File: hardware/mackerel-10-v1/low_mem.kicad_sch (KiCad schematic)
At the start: 8 parts, among them U3 SST39SF040, U4 AS6C4008-55PCN, U5 SST39SF040, U6 AS6C4008-55PCN

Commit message: Another layout plan
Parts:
- removed C1, C2, C3, C4: 0.1uF, Capacitor_THT:C_Disc_D4.7mm_W2.5mm_P5.00mm, symbol Device:C

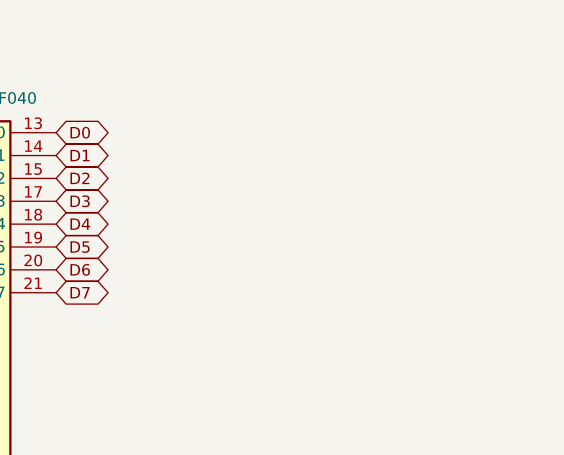
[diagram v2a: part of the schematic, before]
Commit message: half routed
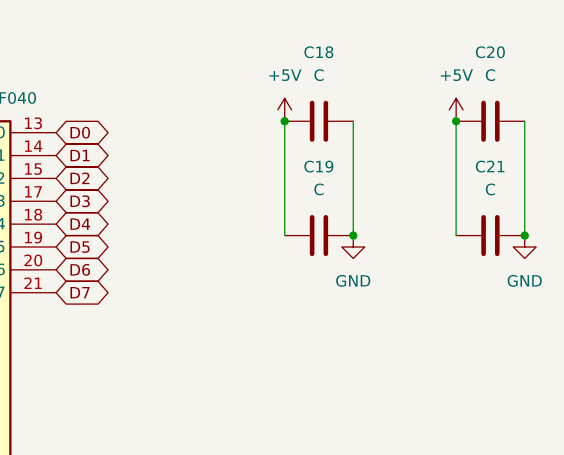
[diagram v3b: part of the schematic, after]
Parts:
- added C18, C19, C20, C21: C, Capacitor_THT:C_Disc_D4.3mm_W1.9mm_P5.00mm, symbol Device:C
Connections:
- net +5V: now also C18.1, C19.1, C20.1, C21.1
- net GND: now also C18.2, C19.2, C20.2, C21.2

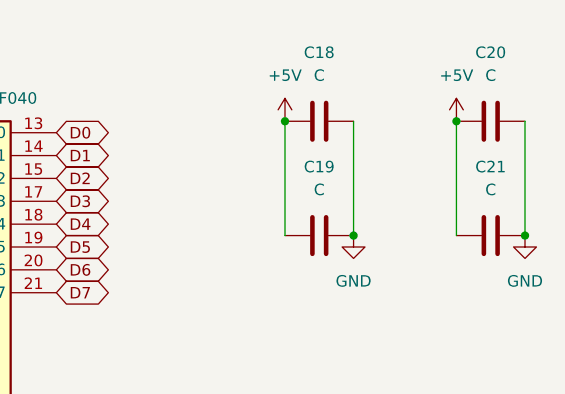
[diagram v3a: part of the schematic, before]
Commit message: Remove BERR from CPLD
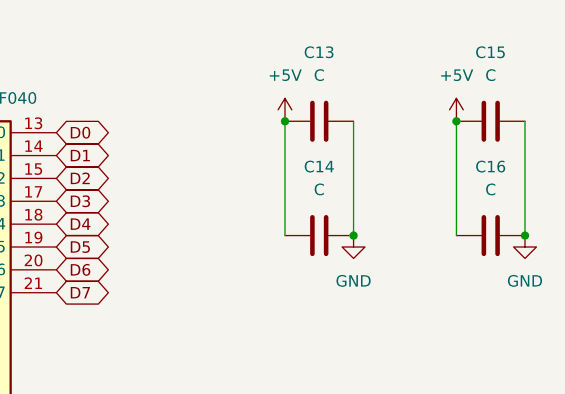
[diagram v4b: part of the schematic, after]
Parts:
- renumbered C18 to C13, C19 to C14, C20 to C15, C21 to C16
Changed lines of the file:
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@@
 		(dnp no)
 		(fields_autoplaced yes)
-		(property "Reference" "#PWR016"
+		(property "Reference" "#PWR025"
 			(at 128.27 34.29 0)
 			(effects
@@
 			(project "mackerel-10-v1"
 				(path "/0a8f74be-008b-4256-a2d9-73a458311ea0/94b238fa-f0c8-40a8-9ec2-3b22cf78cf25"
-					(reference "#PWR016")
+					(reference "#PWR025")
 					(unit 1)
 				)
@@
 		(dnp no)
 		(fields_autoplaced yes)
-		(property "Reference" "#PWR012"
+		(property "Reference" "#PWR021"
 			(at 49.53 111.76 0)
 			(effects
@@
 			(project "mackerel-10-v1"
 				(path "/0a8f74be-008b-4256-a2d9-73a458311ea0/94b238fa-f0c8-40a8-9ec2-3b22cf78cf25"
-					(reference "#PWR012")
+					(reference "#PWR021")
 					(unit 1)
 				)
@@
 		(dnp no)
 		(fields_autoplaced yes)
-		(property "Reference" "#PWR018"
+		(property "Reference" "#PWR027"
 			(at 128.27 128.27 0)
 			(effects
@@
 			(project "mackerel-10-v1"
 				(path "/0a8f74be-008b-4256-a2d9-73a458311ea0/94b238fa-f0c8-40a8-9ec2-3b22cf78cf25"
-					(reference "#PWR018")
+					(reference "#PWR027")
 					(unit 1)
 				)
@@
 		(dnp no)
 		(fields_autoplaced yes)
-		(property "Reference" "#PWR019"
+		(property "Reference" "#PWR028"
 			(at 128.27 191.77 0)
 			(effects
@@
 			(project "mackerel-10-v1"
 				(path "/0a8f74be-008b-4256-a2d9-73a458311ea0/94b238fa-f0c8-40a8-9ec2-3b22cf78cf25"
-					(reference "#PWR019")
+					(reference "#PWR028")
 					(unit 1)
 				)
@@
 		(dnp no)
 		(fields_autoplaced yes)
-		(property "Reference" "#PWR013"
+		(property "Reference" "#PWR022"
 			(at 49.53 128.27 0)
 			(effects
@@
 			(project "mackerel-10-v1"
 				(path "/0a8f74be-008b-4256-a2d9-73a458311ea0/94b238fa-f0c8-40a8-9ec2-3b22cf78cf25"
-					(reference "#PWR013")
+					(reference "#PWR022")
 					(unit 1)
 				)
@@
 		(dnp no)
 		(fields_autoplaced yes)
-		(property "Reference" "#PWR059"
+		(property "Reference" "#PWR031"
 			(at 187.96 39.37 0)
 			(effects
@@
 			(project "mackerel-10-v1"
 				(path "/0a8f74be-008b-4256-a2d9-73a458311ea0/94b238fa-f0c8-40a8-9ec2-3b22cf78cf25"
-					(reference "#PWR059")
+					(reference "#PWR031")
 					(unit 1)
 				)
@@
 		(dnp no)
 		(fields_autoplaced yes)
-		(property "Reference" "#PWR015"
+		(property "Reference" "#PWR024"
 			(at 104.14 91.44 0)
 			(effects
@@
 			(project "mackerel-10-v1"
 				(path "/0a8f74be-008b-4256-a2d9-73a458311ea0/94b238fa-f0c8-40a8-9ec2-3b22cf78cf25"
-					(reference "#PWR015")
+					(reference "#PWR024")
 					(unit 1)
 				)
@@
 		(dnp no)
 		(fields_autoplaced yes)
-		(property "Reference" "C21"
+		(property "Reference" "C16"
 			(at 191.77 40.64 90)
 			(effects
@@
 			(project "mackerel-10-v1"
 				(path "/0a8f74be-008b-4256-a2d9-73a458311ea0/94b238fa-f0c8-40a8-9ec2-3b22cf78cf25"
-					(reference "C21")
+					(reference "C16")
 					(unit 1)
 				)
@@
 		(dnp no)
 		(fields_autoplaced yes)
-		(property "Reference" "#PWR017"
+		(property "Reference" "#PWR026"
 			(at 128.27 113.03 0)
 			(effects
@@
 			(project "mackerel-10-v1"
 				(path "/0a8f74be-008b-4256-a2d9-73a458311ea0/94b238fa-f0c8-40a8-9ec2-3b22cf78cf25"
-					(reference "#PWR017")
+					(reference "#PWR026")
 					(unit 1)
 				)
@@
 		(dnp no)
 		(fields_autoplaced yes)
-		(property "Reference" "#PWR010"
+		(property "Reference" "#PWR019"
 			(at 25.4 91.44 0)
 			(effects
@@
 			(project "mackerel-10-v1"
 				(path "/0a8f74be-008b-4256-a2d9-73a458311ea0/94b238fa-f0c8-40a8-9ec2-3b22cf78cf25"
-					(reference "#PWR010")
+					(reference "#PWR019")
 					(unit 1)
 				)
@@
 		(dnp no)
 		(fields_autoplaced yes)
-		(property "Reference" "C20"
+		(property "Reference" "C15"
 			(at 191.77 27.94 90)
 			(effects
@@
 			(project "mackerel-10-v1"
 				(path "/0a8f74be-008b-4256-a2d9-73a458311ea0/94b238fa-f0c8-40a8-9ec2-3b22cf78cf25"
-					(reference "C20")
+					(reference "C15")
 					(unit 1)
 				)
@@
 		(dnp no)
 		(fields_autoplaced yes)
-		(property "Reference" "#PWR014"
+		(property "Reference" "#PWR023"
 			(at 49.53 191.77 0)
 			(effects
@@
 			(project "mackerel-10-v1"
 				(path "/0a8f74be-008b-4256-a2d9-73a458311ea0/94b238fa-f0c8-40a8-9ec2-3b22cf78cf25"
-					(reference "#PWR014")
+					(reference "#PWR023")
 					(unit 1)
 				)
@@
 		(dnp no)
 		(fields_autoplaced yes)
-		(property "Reference" "#PWR050"
+		(property "Reference" "#PWR029"
 			(at 168.91 39.37 0)
 			(effects
@@
 			(project "mackerel-10-v1"
 				(path "/0a8f74be-008b-4256-a2d9-73a458311ea0/94b238fa-f0c8-40a8-9ec2-3b22cf78cf25"
-					(reference "#PWR050")
+					(reference "#PWR029")
 					(unit 1)
 				)
@@
 		(dnp no)
 		(fields_autoplaced yes)
-		(property "Reference" "#PWR060"
+		(property "Reference" "#PWR032"
 			(at 195.58 54.61 0)
 			(effects
@@
 			(project "mackerel-10-v1"
 				(path "/0a8f74be-008b-4256-a2d9-73a458311ea0/94b238fa-f0c8-40a8-9ec2-3b22cf78cf25"
-					(reference "#PWR060")
+					(reference "#PWR032")
 					(unit 1)
 				)
@@
 		(dnp no)
 		(fields_autoplaced yes)
-		(property "Reference" "#PWR011"
+		(property "Reference" "#PWR020"
 			(at 49.53 34.29 0)
 			(effects
@@
 			(project "mackerel-10-v1"
 				(path "/0a8f74be-008b-4256-a2d9-73a458311ea0/94b238fa-f0c8-40a8-9ec2-3b22cf78cf25"
-					(reference "#PWR011")
+					(reference "#PWR020")
 					(unit 1)
 				)
@@
 		(dnp no)
 		(fields_autoplaced yes)
-		(property "Reference" "#PWR051"
+		(property "Reference" "#PWR030"
 			(at 176.53 54.61 0)
 			(effects
@@
 			(project "mackerel-10-v1"
 				(path "/0a8f74be-008b-4256-a2d9-73a458311ea0/94b238fa-f0c8-40a8-9ec2-3b22cf78cf25"
-					(reference "#PWR051")
+					(reference "#PWR030")
 					(unit 1)
 				)
@@
 		(dnp no)
 		(fields_autoplaced yes)
-		(property "Reference" "C18"
+		(property "Reference" "C13"
 			(at 172.72 27.94 90)
 			(effects
@@
 			(project "mackerel-10-v1"
 				(path "/0a8f74be-008b-4256-a2d9-73a458311ea0/94b238fa-f0c8-40a8-9ec2-3b22cf78cf25"
-					(reference "C18")
+					(reference "C13")
 					(unit 1)
 				)
@@
 		(dnp no)
 		(fields_autoplaced yes)
-		(property "Reference" "C19"
+		(property "Reference" "C14"
 			(at 172.72 40.64 90)
 			(effects
@@
 			(project "mackerel-10-v1"
 				(path "/0a8f74be-008b-4256-a2d9-73a458311ea0/94b238fa-f0c8-40a8-9ec2-3b22cf78cf25"
-					(reference "C19")
-					(unit 1)
-				)
+					(reference "C14")
+					(unit 1)
+				)

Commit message: Mackerel-10 v1.1 release PCB
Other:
- title: Mackerel-10 SBC v1 -> Mackerel-10 SBC v1.1
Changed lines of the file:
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@@
 	(paper "A")
 	(title_block
-		(title "Mackerel-10 SBC v1")
-		(date "2024-09-23")
-		(rev "1.0a")
+		(title "Mackerel-10 SBC v1.1")
+		(date "2024-10-27")
+		(rev "1.1a")
 		(company "Colin Maykish")
 	)

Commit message: Add Mackerel-10 v1.1 BOM
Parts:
- C13, C14, C15, C16: value C -> 0.1uF
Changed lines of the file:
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@@
 			)
 		)
-		(property "Value" "C"
+		(property "Value" "0.1uF"
 			(at 191.77 43.18 90)
 			(effects
@@
 			)
 		)
-		(property "Value" "C"
+		(property "Value" "0.1uF"
 			(at 191.77 30.48 90)
 			(effects
@@
 			)
 		)
-		(property "Value" "C"
+		(property "Value" "0.1uF"
 			(at 172.72 30.48 90)
 			(effects
@@
 			)
 		)
-		(property "Value" "C"
+		(property "Value" "0.1uF"
 			(at 172.72 43.18 90)
 			(effects

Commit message: Mackerel-10 v1.2 Gerber release
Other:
- title: Mackerel-10 SBC v1.1 -> Mackerel-10
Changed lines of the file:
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@@
 	(paper "A")
 	(title_block
-		(title "Mackerel-10 SBC v1.1")
-		(date "2024-10-27")
-		(rev "1.1a")
+		(title "Mackerel-10")
+		(date "2024-11-09")
+		(rev "1.2")
 		(company "Colin Maykish")
 	)
